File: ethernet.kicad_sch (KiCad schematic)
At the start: 37 parts, among them IC1 ACPL-217-500E, J6 5-2337992-8, U22 TPS2372-3RGWR, U23 ULS-12{slash}5-D48N-C

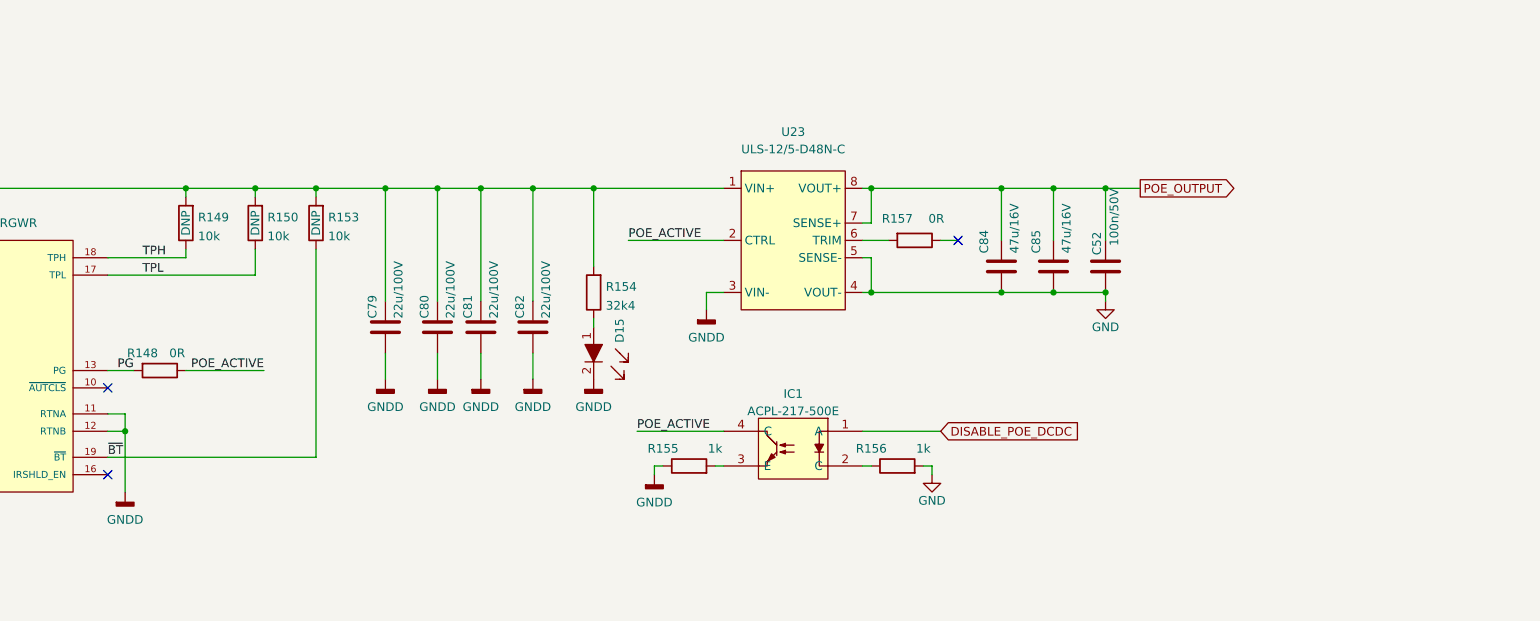
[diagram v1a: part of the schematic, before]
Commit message: Fixed PoE enable signalling [#40391]
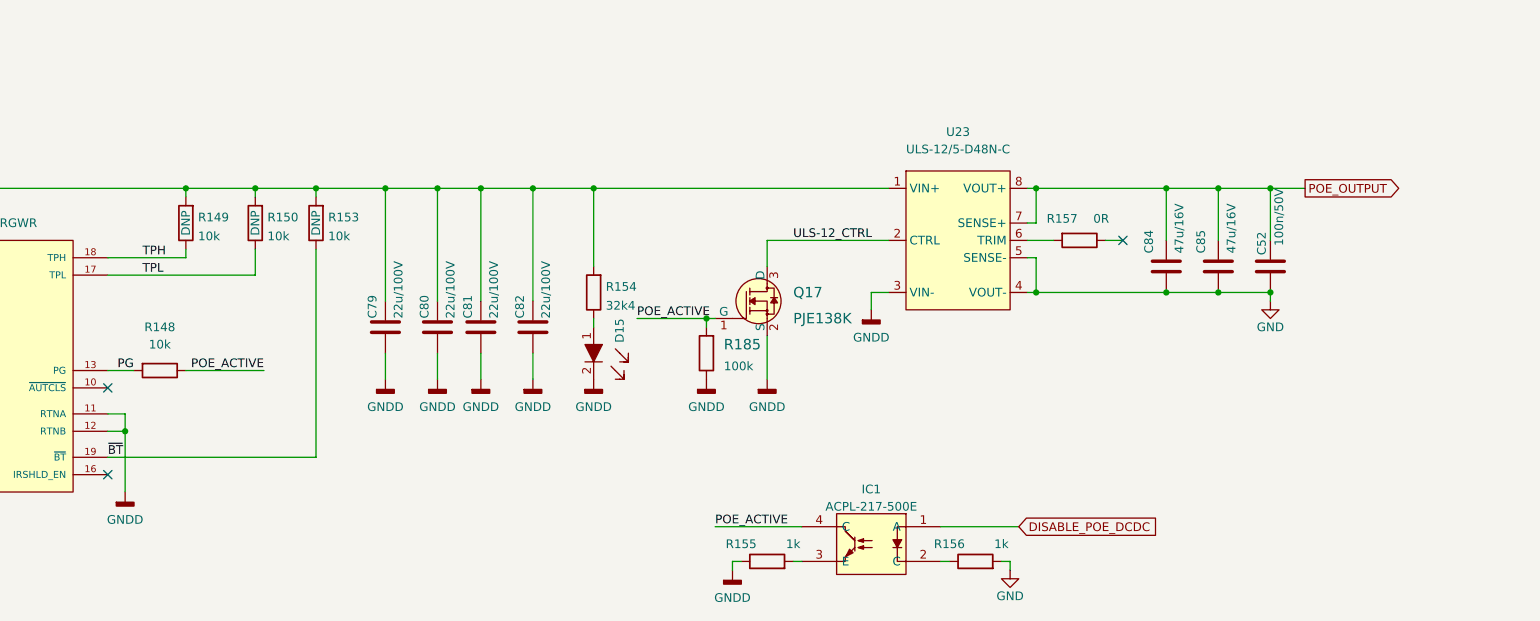
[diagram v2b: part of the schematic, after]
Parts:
- added Q17: PJE138K, antmicro-footprints:SOT-523, symbol antmicroTransistorsFETsMOSFETsSingle:PJE138K
- added R185: R_100k_0402, antmicro-footprints:0402-res, symbol antmicroResistors0402:R_100k_0402
- R148: value R_0R_0402 -> R_10k_0402; symbol jetson-orin-baseboard:R_0R_0402 -> jetson-orin-baseboard:R_10k_0402; MPN ERJ2GE0R00X -> CRCW040210K0FKEDHP; Manufacturer PANASONIC -> VISHAY; Val 0R -> 10k
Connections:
- net GNDD: now also Q17.2 (S), R185.1
- net POE_ACTIVE: now also Q17.1 (G), R185.2; no longer U23.2 (CTRL)
- new net ULS-12_CTRL: Q17.3 (D), U23.2 (CTRL)
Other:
- moved on the sheet: C52, C84, C85, IC1, R155, R156, R157, U23

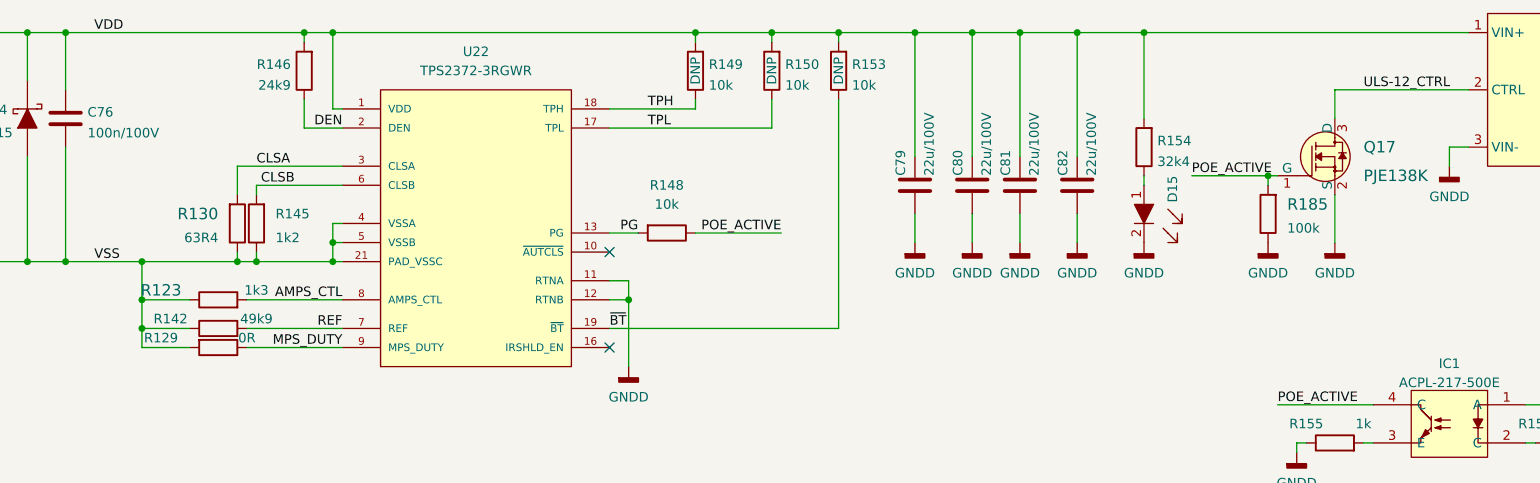
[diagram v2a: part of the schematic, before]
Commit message: Replaced PCA9547 with PI4MSD5V9548AZDEX to support 1.8V I2C voltages for cameras [#40392]
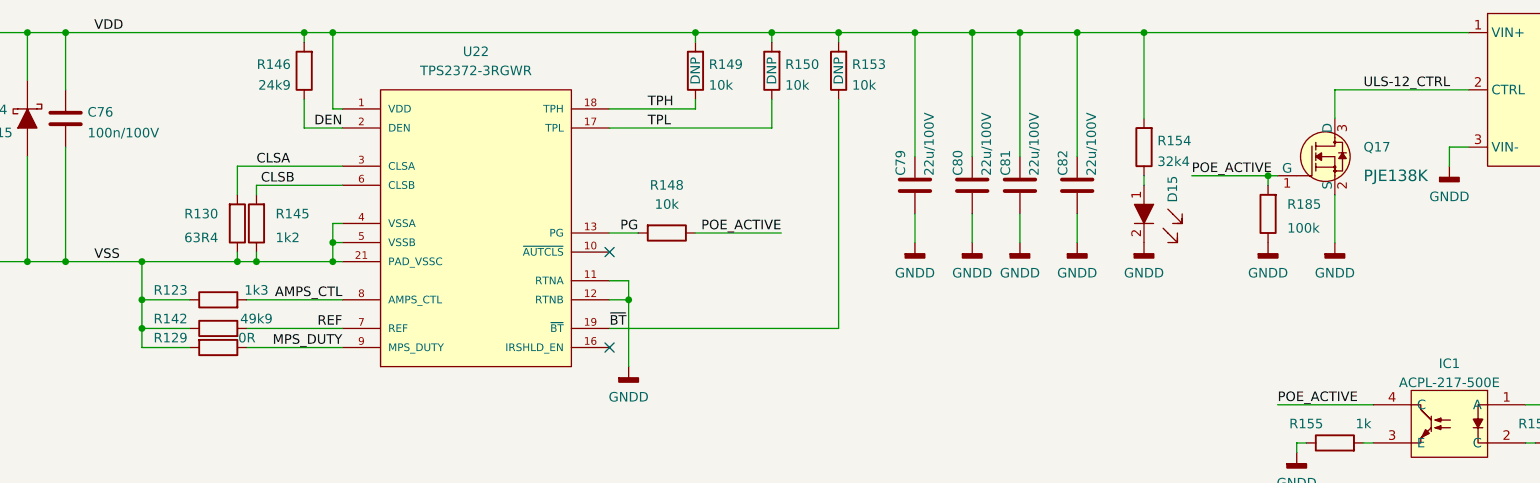
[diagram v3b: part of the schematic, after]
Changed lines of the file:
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@@
     (in_bom yes) (on_board yes) (fields_autoplaced)
     (property "Reference" "Q17" (id 0) (at 294.64 196.85 0)
-      (effects (font (size 1.524 1.524)) (justify left))
+      (effects (font (size 1.27 1.27)) (justify left))
     )
     (property "Value" "PJE138K" (id 1) (at 294.64 200.66 0)
@@
     (in_bom yes) (on_board yes) (fields_autoplaced)
     (property "Reference" "R130" (id 0) (at 142.24 205.74 90)
-      (effects (font (size 1.524 1.524)) (justify right))
+      (effects (font (size 1.27 1.27)) (justify right))
     )
     (property "Value" "R_63R4_0402" (id 1) (at 140.97 207.01 0)
@@
   (symbol (lib_id "jetson-orin-baseboard:R_0R_0402") (at 142.24 223.52 180) (unit 1)
     (in_bom yes) (on_board yes)
-    (property "Reference" "R129" (id 0) (at 134.62 222.25 0))
+    (property "Reference" "R129" (id 0) (at 135.89 222.25 0))
     (property "Value" "R_0R_0402" (id 1) (at 142.24 219.71 0)
       (effects (font (size 1.524 1.524)) hide)
@@
     (in_bom yes) (on_board yes) (fields_autoplaced)
     (property "Reference" "R185" (id 0) (at 284.48 204.47 90)
-      (effects (font (size 1.524 1.524)) (justify right))
+      (effects (font (size 1.27 1.27)) (justify right))
     )
     (property "Value" "R_100k_0402" (id 1) (at 285.75 205.74 0)
@@
   (symbol (lib_id "jetson-orin-baseboard:R_1k3_0402") (at 142.24 217.17 0) (unit 1)
     (in_bom yes) (on_board yes)
-    (property "Reference" "R123" (id 0) (at 134.62 215.9 0)
-      (effects (font (size 1.524 1.524)))
-    )
+    (property "Reference" "R123" (id 0) (at 135.89 215.9 0))
     (property "Value" "R_1k3_0402" (id 1) (at 144.78 203.2 0)
       (effects (font (size 1.524 1.524)) (justify left bottom) hide)

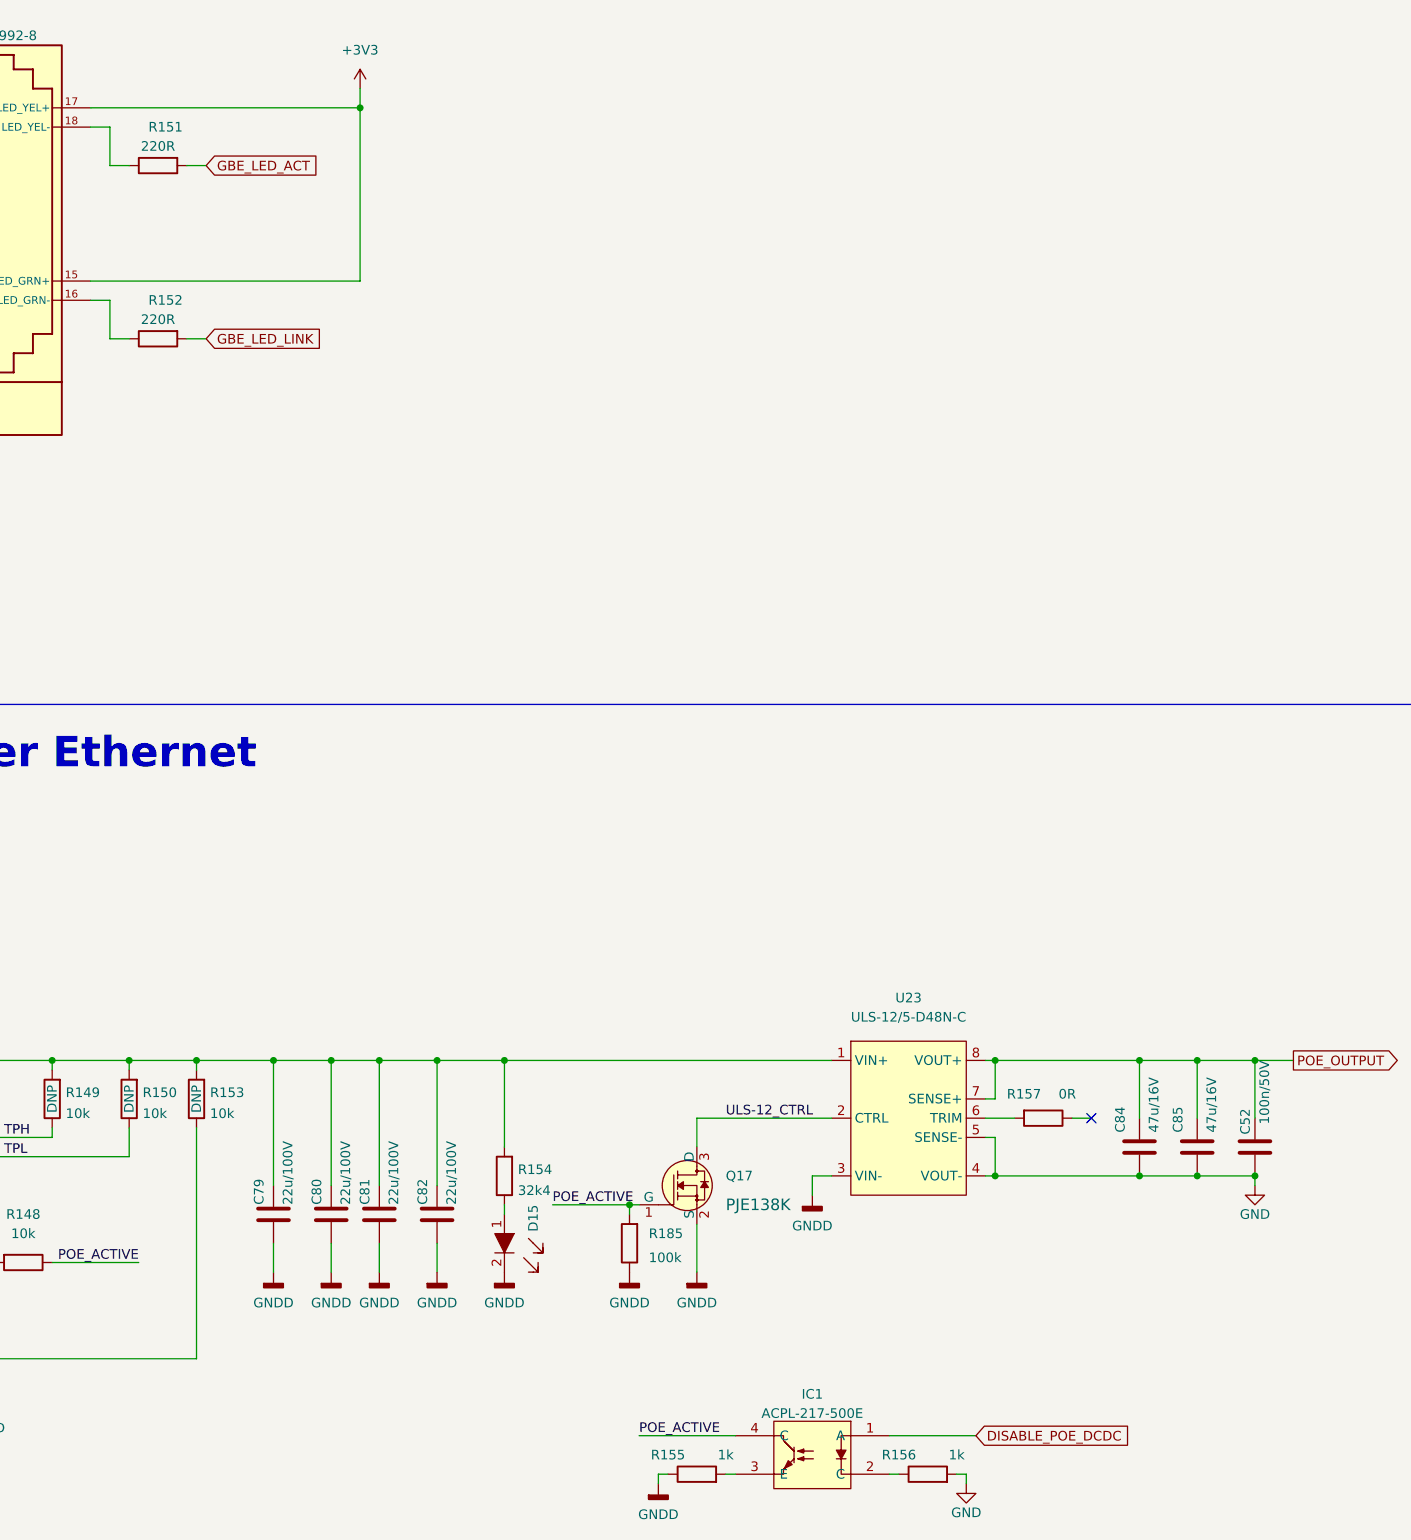
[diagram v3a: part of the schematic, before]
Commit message: BOM reduction [#40581]
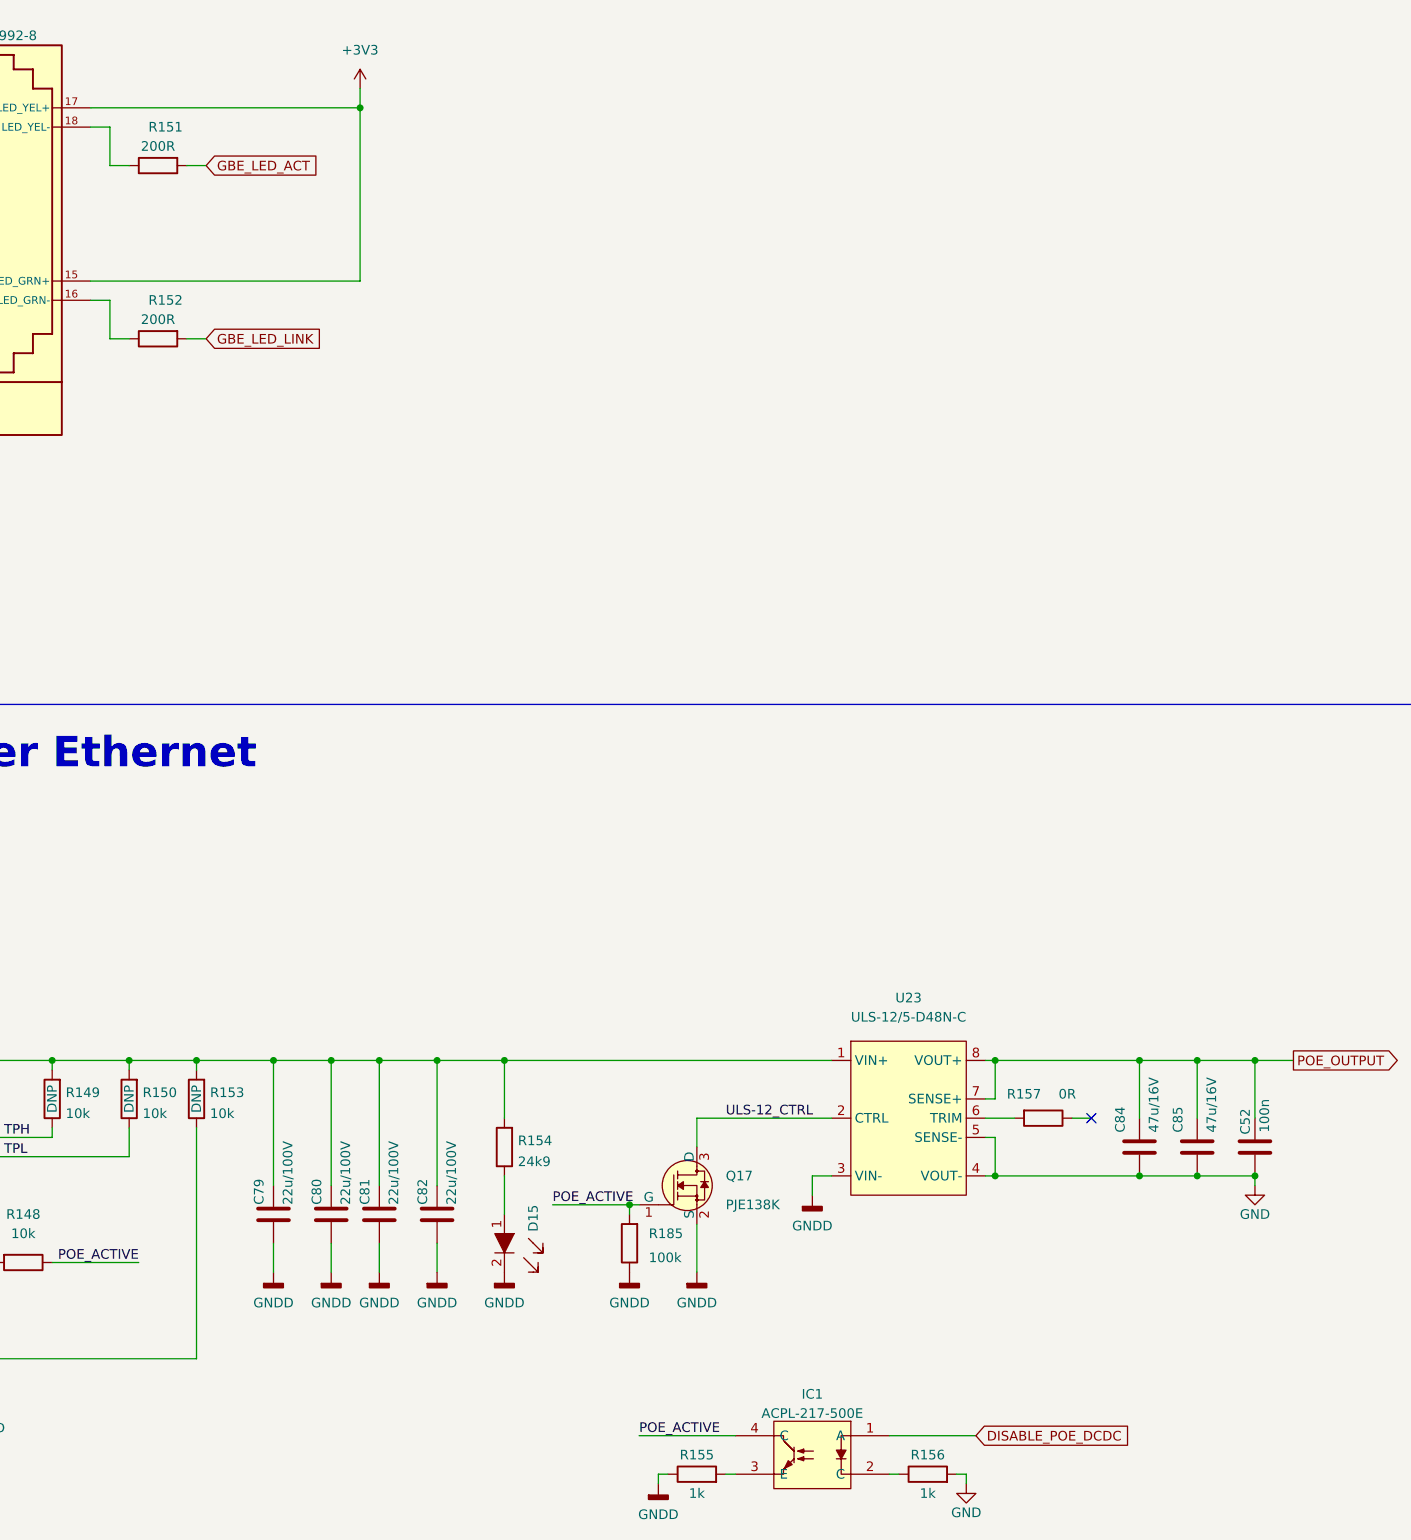
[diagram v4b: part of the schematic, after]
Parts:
- removed R155, R156: R_1k_0603, jetson-orin-baseboard-footprints:0603-res, symbol jetson-orin-baseboard:R_1k_0603
- added R155, R156: R_1k_0402, antmicro-footprints:0402-res, symbol antmicroResistors0402:R_1k_0402
- C52: value C_100n_0402_50V -> C_100n_0402; symbol jetson-orin-baseboard:C_100n_0402_50V -> jetson-orin-baseboard:C_100n_0402; MPN GRM155R71H104KE14D -> GRM155R61H104KE14D; Manufacturer MURATA -> Murata; Val 100n/50V -> 100n
- R151, R152: value R_220R_0402 -> R_200R_0402; symbol jetson-orin-baseboard:R_220R_0402 -> jetson-orin-baseboard:R_200R_0402; MPN ERJ2GEJ221X -> RC0402FR-07200RL; Manufacturer Panasonic -> YAGEO; Val 220R -> 200R
- R154: value R_32k4_0402 -> R_24k9_0402; symbol jetson-orin-baseboard:R_32k4_0402 -> jetson-orin-baseboard:R_24k9_0402; MPN ERA-2ARB3242X -> WR04X2492FTL; Manufacturer PANASONIC_ELECTRONIC_COMPONENTS -> WALSIN; Val 32k4 -> 24k9
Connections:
- net GND: now also R156.2
- net GNDD: now also R155.1
- net at IC1.2 (C): now also R156.1
- net at IC1.3 (E): now also R155.2
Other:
- moved on the sheet: R154
